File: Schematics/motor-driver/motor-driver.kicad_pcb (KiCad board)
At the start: 2 copper layers, 99.1 x 74.9 mm, 40 parts, among them J1 XT-60, J10 I2C/Ain/PWM 5V, J11 PWM/PPM 5V, J2 SPI, J3 32-33, J4 UART/I2C/PWM 3.3V, J5 I2C/Ain/PWM 3.3V, J6 PWM/PPM 3.3V, J7 UART/Ain, J8 32-33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

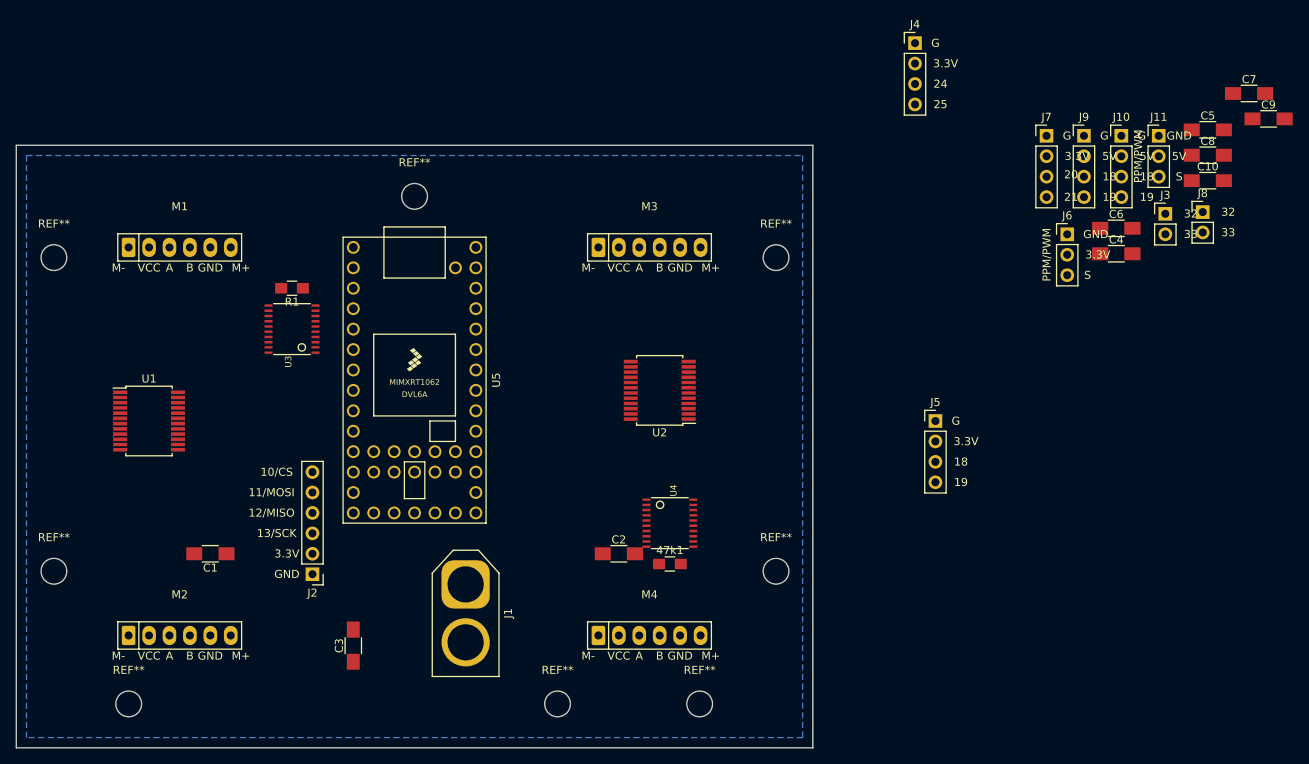
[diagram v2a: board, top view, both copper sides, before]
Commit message: Finish updating motor driver PCB for Teensy 4.0
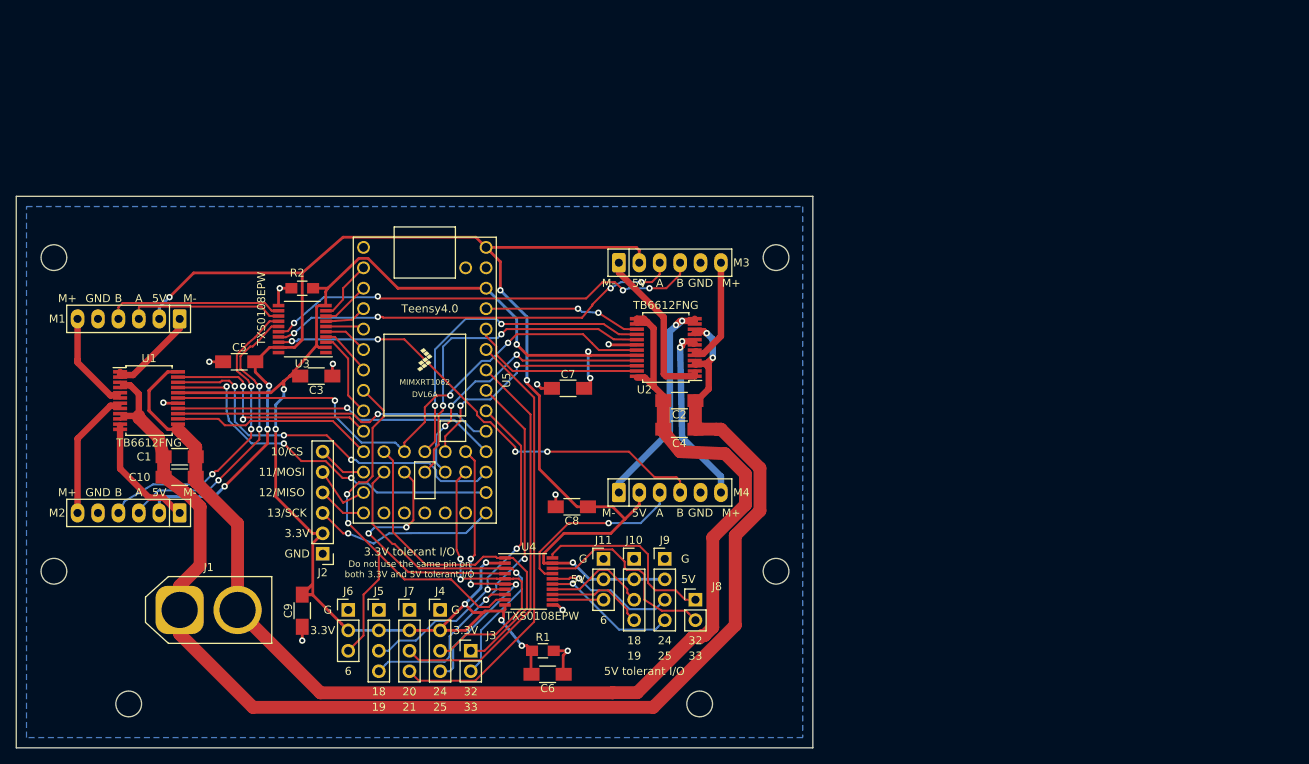
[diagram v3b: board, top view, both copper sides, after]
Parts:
- removed the R1 at (73.7, 54.6)
- removed the REF** at (106.7, 106.3)
- removed the REF** at (88.9, 43.2)
- added R2: 47k, Resistors_SMD:R_0805_HandSoldering, F.Cu at (74.9, 54.6)
- J3: value 32-33 -> 32-33 3.3V
- J8: value 32-33 -> 32-33 5V
- J9: footprint Rover:I2C_Ain_PWM_5V -> Rover:UART_I2C_PWM_5V
- R1: renamed from 47k1; value R -> 47k
- U3, U4: value TXB0108PWR -> TXS0108EPW; footprint TXB0108PWR:TSSOP20 -> Housings_SSOP:TSSOP-20_4.4x6.5mm_Pitch0.65mm
- moved C9 134.8 mm to (74.9, 94.7), turned to 90 degrees
- moved C10 133.1 mm to (59.7, 78.1)
- moved C5 123.9 mm to (67.1, 63.8), turned to 180 degrees
- moved J3 102.0 mm to (95.9, 99.7)
- moved J6 100.9 mm to (80.6, 94.6)
- moved J7 98.8 mm to (88.3, 94.6)
- moved C7 92.3 mm to (108.0, 67.1)
- moved J4 92.0 mm to (92.1, 94.6)
- moved C8 90.4 mm to (108.5, 81.8), turned to 180 degrees
- moved C6 89.9 mm to (105.4, 102.6), turned to 180 degrees
- moved J11 86.8 mm to (112.4, 88.3)
- moved J10 80.2 mm to (116.2, 88.3)
- moved J8 79.4 mm to (123.8, 93.3)
- moved J9 74.1 mm to (120.0, 88.3)
- moved J5 73.1 mm to (84.5, 94.6)
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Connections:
- J4 pad 1: Net-(J4-Pad1) -> GND
- J4 pad 2: Net-(J4-Pad2) -> +3V3
- J4 pad 3: +5V -> Net-(J4-Pad3)
- J4 pad 4: GND -> Net-(J4-Pad4)
- J6 pad 2: +5V -> +3V3
- J9 pad 1: Net-(J9-Pad1) -> GND
- J9 pad 2: Net-(J9-Pad2) -> +5V
- J9 pad 3: +5V -> Net-(J9-Pad3)
- J9 pad 4: GND -> Net-(J9-Pad4)
- U4 pad 15: Net-(J9-Pad2) -> Net-(J9-Pad4)
- U4 pad 16: Net-(J9-Pad1) -> Net-(J9-Pad3)
- U4 pad 5: Net-(J4-Pad1) -> Net-(J4-Pad3)
- U4 pad 6: Net-(J4-Pad2) -> Net-(J4-Pad4)
- U5 pad 35: Net-(J4-Pad2) -> Net-(J4-Pad3)
- U5 pad 36: Net-(J4-Pad1) -> Net-(J4-Pad4)
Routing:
- net +5V: track 0.00 -> 188.2 mm, vias 0 -> 7
- net +3V3: track 0.00 -> 172.1 mm, vias 0 -> 9
- net -BATT: track 0.00 -> 165.8 mm, vias 0 -> 2
- net +BATT: track 0.00 -> 157.3 mm
- net STBY: track 0.00 -> 69.8 mm, vias 0 -> 3
- net Net-(M4-Pad4): track 0.00 -> 59.4 mm, vias 0 -> 4
- net Net-(J6-Pad3): track 0.00 -> 57.9 mm, vias 0 -> 2
- net Net-(J7-Pad4): track 0.00 -> 55.4 mm
- net Net-(M3-Pad4): track 0.00 -> 55.2 mm, vias 0 -> 4
- net Net-(M3-Pad3): track 0.00 -> 52.0 mm, vias 0 -> 4
- net Net-(J5-Pad4): track 0.00 -> 51.4 mm, vias 0 -> 2
- net Net-(J7-Pad3): track 0.00 -> 50.3 mm
- net Net-(U1-Pad22): track 0.00 -> 47.1 mm, vias 0 -> 3
- net Net-(U1-Pad21): track 0.00 -> 46.0 mm, vias 0 -> 3
- net Net-(J5-Pad3): track 0.00 -> 44.6 mm, vias 0 -> 2
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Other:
- board size 99.1 x 74.9 mm -> 99.1 x 68.6 mm
- board text added: "3.3V tolerant I/O"
- board text added: "5V tolerant I/O"
- board text added: "Do not use the same pin on both 3.3V and 5V tolerant I/O"
